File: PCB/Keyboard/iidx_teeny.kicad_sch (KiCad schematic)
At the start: 46 parts, among them J1 CONN_01x05, SW1 SWITCH_SPST, SW10 SWITCH_SPST, SW11 SWITCH_SPST, SW12 SWITCH_SPST, SW13 SWITCH_SPST, SW2 SWITCH_SPST, SW3 SWITCH_SPST, SW4 SWITCH_SPST, SW5 SWITCH_SPST, SW6 SWITCH_SPST, SW7 SWITCH_SPST, SW8 SWITCH_SPST, SW9 SWITCH_SPST, U1 Pico, U2 SN74LV1T34DBV, U3 SN74LV1T34DBV

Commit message: PCB and keyboard housing done
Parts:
- removed J1: CONN_01x05, iidx_pico:Pogo_5P_Female, symbol agg:CONN_01x05
- removed TV1, TV2, TV3: D_TVS, Diode_SMD:D_SOD-323_HandSoldering, symbol Device:D_TVS
- added J1: Conn_01x03, iidx_teeny:Solder_3P, symbol Connector_Generic:Conn_01x03
- added J2: Conn_01x04, iidx_teeny:Solder_4P, symbol Connector_Generic:Conn_01x04
- D1: renamed from D10; footprint iidx_pico:WS2812B-2835 -> iidx_teeny:WS2812B-2835; symbol iidx_pico:WS2812B_Unified -> iidx_teeny:WS2812B_Unified
- D2: renamed from D20; footprint iidx_pico:WS2812B-2835 -> iidx_teeny:WS2812B-2835; symbol iidx_pico:WS2812B_Unified -> iidx_teeny:WS2812B_Unified
- D3: renamed from D30; footprint iidx_pico:WS2812B-2835 -> iidx_teeny:WS2812B-2835; symbol iidx_pico:WS2812B_Unified -> iidx_teeny:WS2812B_Unified
- D4: renamed from D40; footprint iidx_pico:WS2812B-2835 -> iidx_teeny:WS2812B-2835; symbol iidx_pico:WS2812B_Unified -> iidx_teeny:WS2812B_Unified
- D5: renamed from D50; footprint iidx_pico:WS2812B-2835 -> iidx_teeny:WS2812B-2835; symbol iidx_pico:WS2812B_Unified -> iidx_teeny:WS2812B_Unified
- D6: renamed from D60; footprint iidx_pico:WS2812B-2835 -> iidx_teeny:WS2812B-2835; symbol iidx_pico:WS2812B_Unified -> iidx_teeny:WS2812B_Unified
- D7: renamed from D70; footprint iidx_pico:WS2812B-2835 -> iidx_teeny:WS2812B-2835; symbol iidx_pico:WS2812B_Unified -> iidx_teeny:WS2812B_Unified
- DA1, DA2, DA3, DA4: footprint iidx_pico:WS2812B-2835 -> iidx_teeny:WS2812B-2835; symbol iidx_pico:WS2812B_Unified -> iidx_teeny:WS2812B_Unified
- SCR1, SCR2, SCR3, SCR4: footprint iidx_pico:MountingHole_3.2mm_M3 -> iidx_teeny:MountingHole_3.2mm_M3; symbol iidx_pico:ScrewHole -> iidx_teeny:ScrewHole
- U2, U3: footprint iidx_pico:SOT-23-5_Jumper -> iidx_teeny:SOT-23-5_Jumper
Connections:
- net +5V: now also J1.1 (Pin_1)
- net GND: now also J1.3 (Pin_3), J2.4 (Pin_4)
- net SCL: now also J2.2 (Pin_2)
- net SDA: now also J2.3 (Pin_3)
- net TT_LED: now also J1.2 (Pin_2)
- net 3V3: now reaches U1.36 (3V3)
- net 3V3: now also J2.1 (Pin_1)
- no-connect marks 14 -> 18
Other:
- moved on the sheet: R1, R3

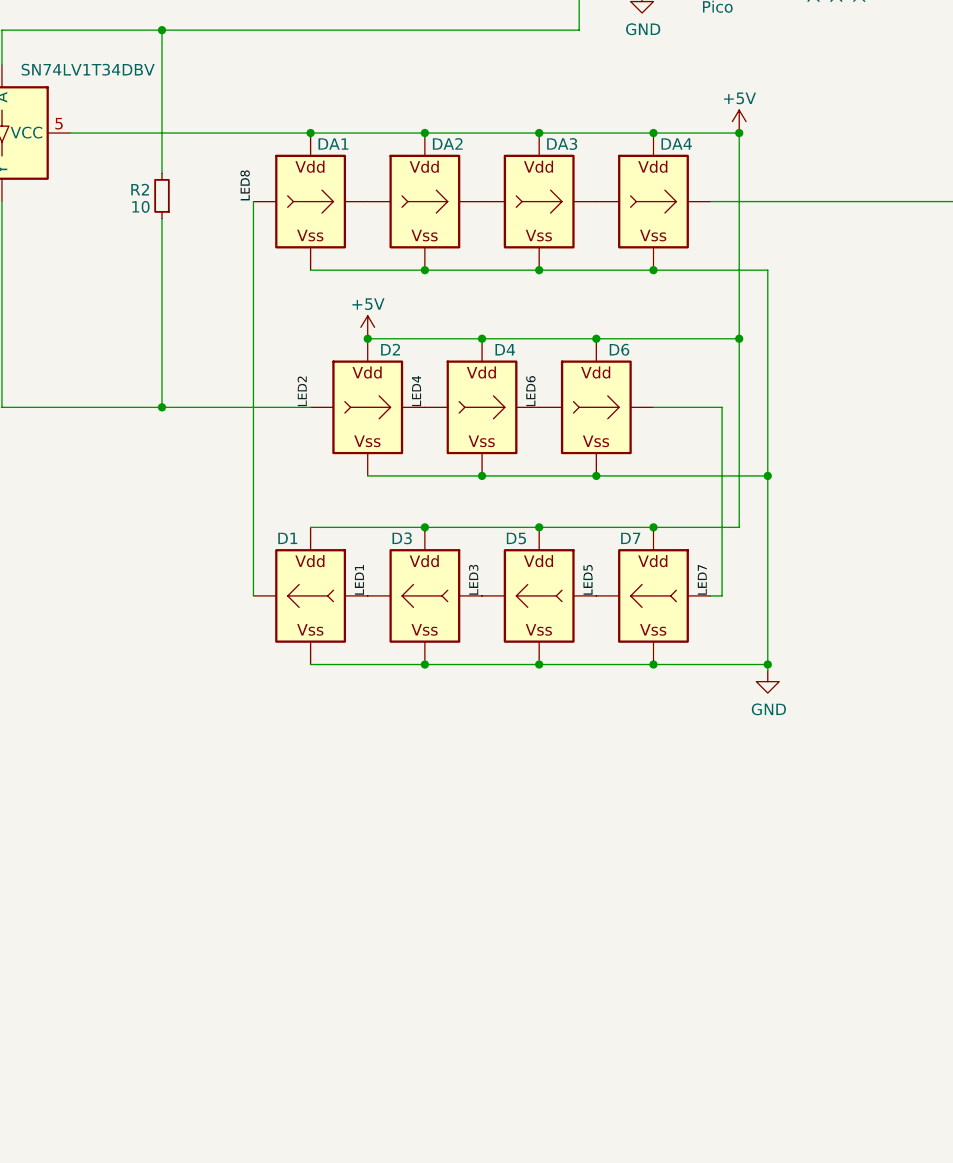
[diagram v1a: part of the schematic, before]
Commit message: PCB updated with two LEDs per button and larger Y gap
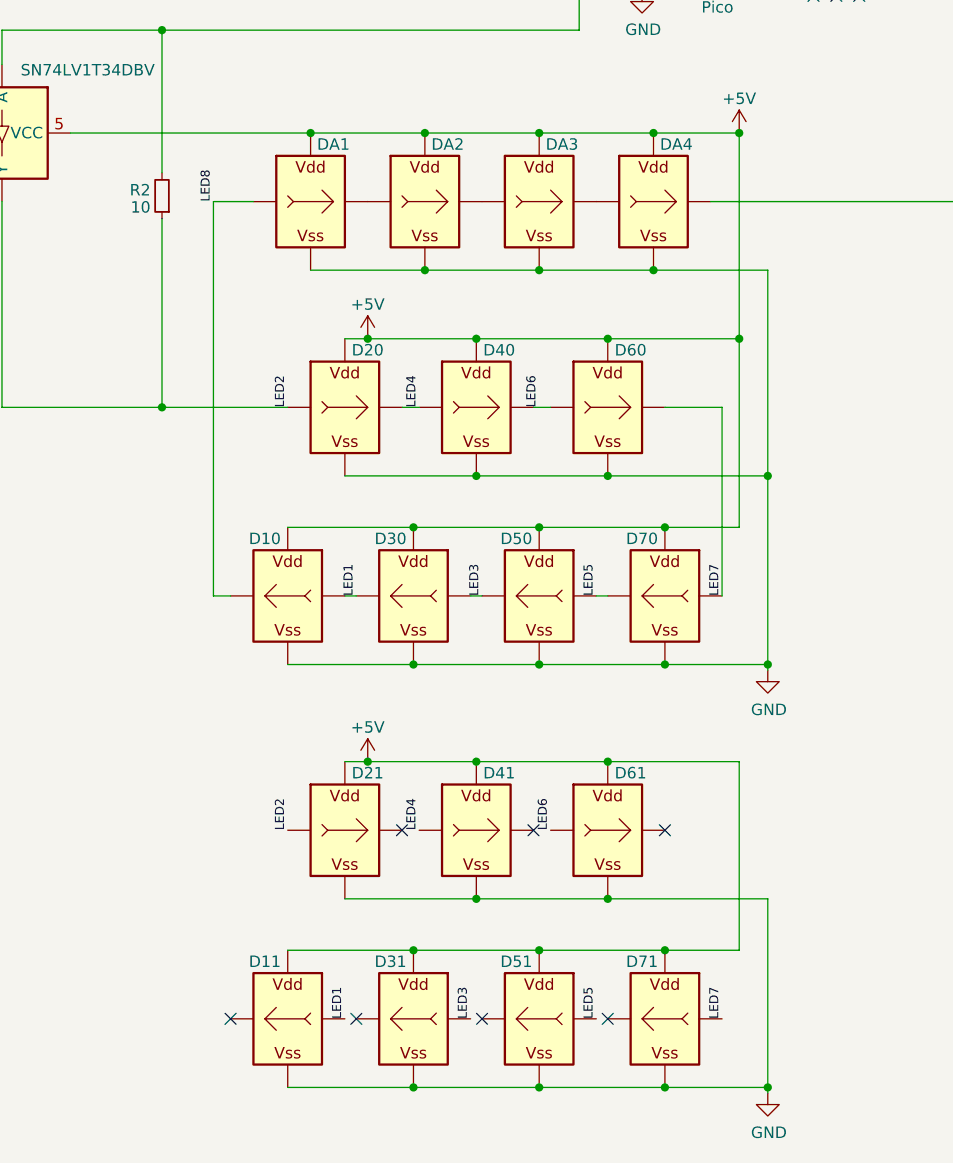
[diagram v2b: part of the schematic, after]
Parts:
- added D11, D21, D31, D41, D51, D61, D71: WS2812B_Unified, iidx_teeny:WS2812B-2835, symbol iidx_teeny:WS2812B_Unified
- renumbered D1 to D10, D2 to D20, D3 to D30, D4 to D40, D5 to D50, D6 to D60, D7 to D70
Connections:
- net +5V: now also D11.V (VDD), D21.V (VDD), D31.V (VDD), D41.V (VDD), D51.V (VDD), D61.V (VDD), D71.V (VDD)
- net GND: now also D11.G (VSS), D21.G (VSS), D31.G (VSS), D41.G (VSS), D51.G (VSS), D61.G (VSS), D71.G (VSS)
- net LED1: now also D11.I (In)
- net LED2: now also D21.I (In)
- net LED3: now also D31.I (In)
- net LED4: now also D41.I (In)
- net LED5: now also D51.I (In)
- net LED6: now also D61.I (In)
- net LED7: now also D71.I (In)
- no-connect marks 18 -> 25
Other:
- moved on the sheet: D10, D20, D30, D40, D60, D70

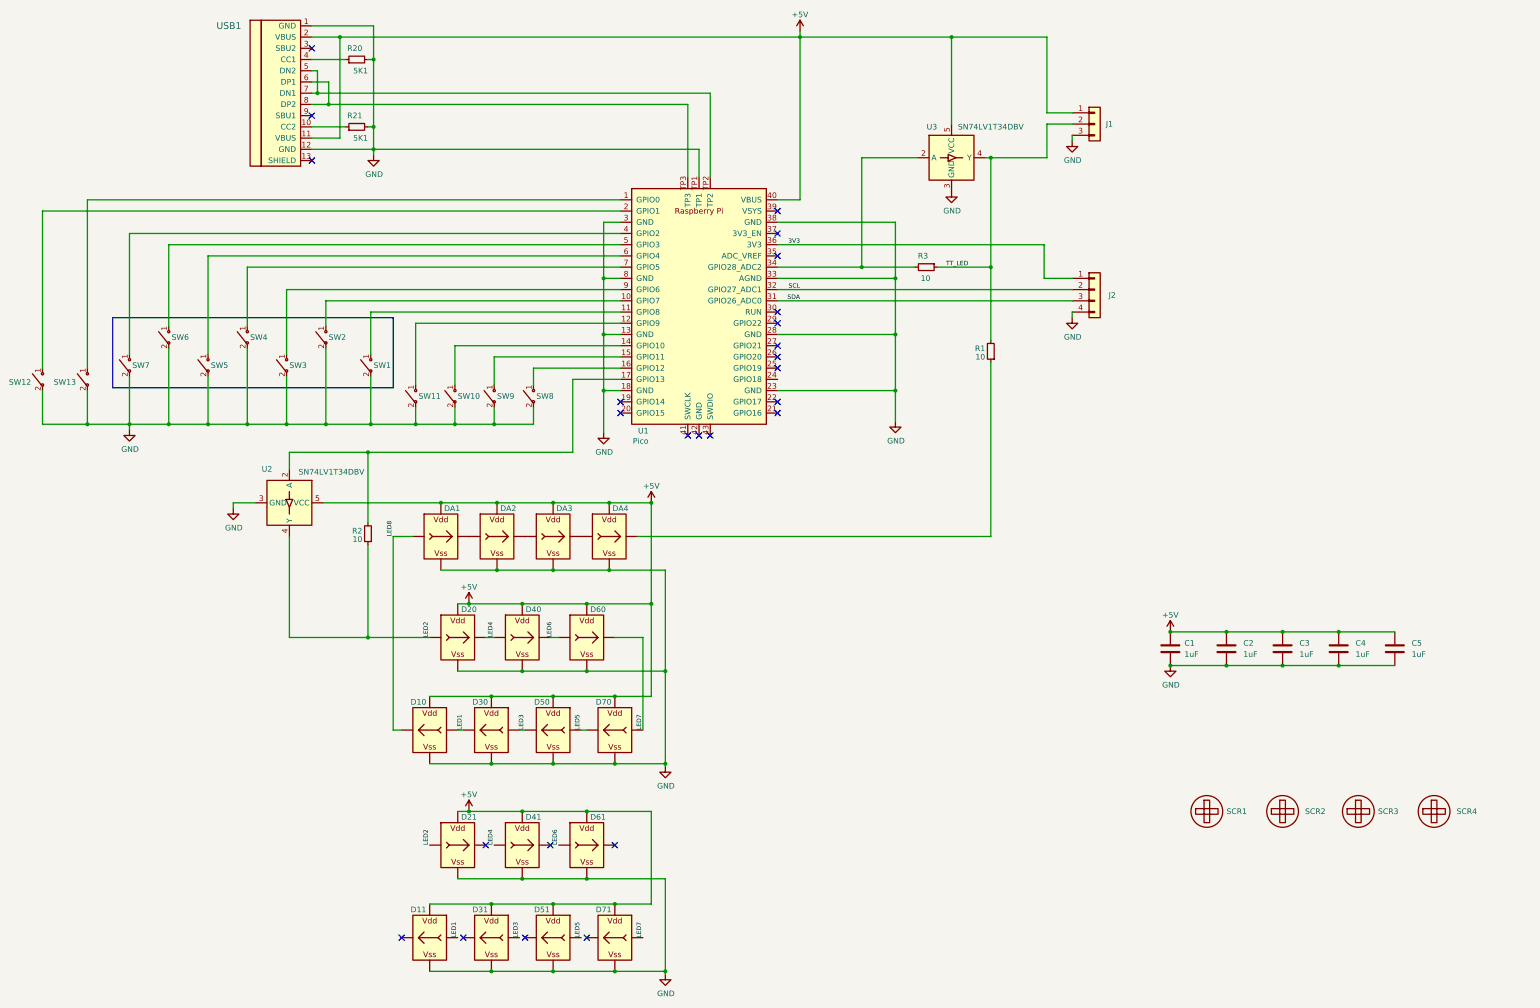
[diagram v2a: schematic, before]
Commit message: PCB v1.2, easier soldering
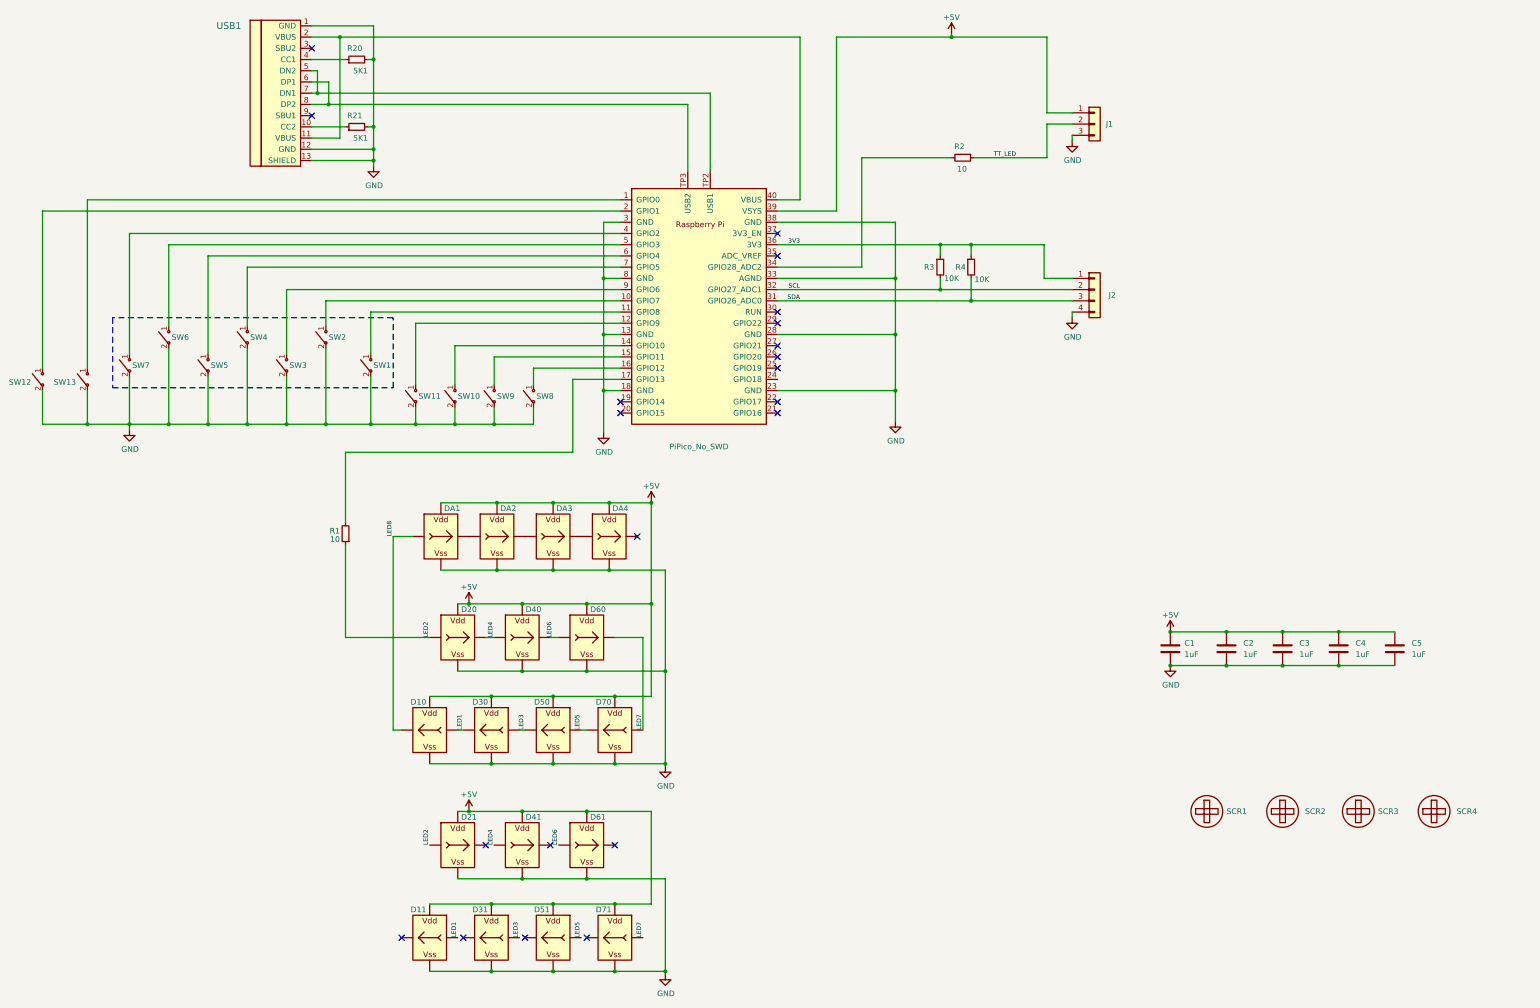
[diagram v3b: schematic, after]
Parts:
- removed R1: 10, Resistor_SMD:R_0603_1608Metric, symbol Device:R_Small
- removed U1: Pico, iidx_teeny:RPi_Pico_SMD_Pins, symbol MCU_RaspberryPi_and_Boards:Pico
- removed U2, U3: SN74LV1T34DBV, iidx_teeny:SOT-23-5_Jumper, symbol Logic_LevelTranslator:SN74LV1T34DBV
- added R3, R4: 10K, Resistor_SMD:R_0603_1608Metric_Pad0.98x0.95mm_HandSolder, symbol Device:R_Small
- added U1: PiPico_No_SWD, iidx_teeny:RPi_Pico_SMD_Pins_No_SWD_No_Text, symbol iidx_pico:PiPico_No_SWD
- R1: renamed from R2; footprint Resistor_SMD:R_0603_1608Metric -> Resistor_SMD:R_0603_1608Metric_Pad0.98x0.95mm_HandSolder
- R2: renamed from R3; footprint Resistor_SMD:R_0603_1608Metric -> Resistor_SMD:R_0603_1608Metric_Pad0.98x0.95mm_HandSolder
- R20, R21: footprint Resistor_SMD:R_0603_1608Metric -> Resistor_SMD:R_0603_1608Metric_Pad0.98x0.95mm_HandSolder
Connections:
- net +5V: now also U1.39 (VSYS); no longer USB1.11 (VBUS), USB1.2 (VBUS)
- net 3V3: now also R3.1, R4.1, U1.36 (3V3)
- net GND: now also USB1.13 (SHIELD), U1.13 (GND), U1.18 (GND), U1.23 (GND), U1.28 (GND), U1.3 (GND), U1.33 (AGND), U1.38 (GND), U1.8 (GND)
- net SCL: now also R3.2, U1.32 (GPIO27_ADC1)
- net SDA: now also R4.2, U1.31 (GPIO26_ADC0)
- net at SW13.1 ("~{"}): now also U1.1 (GPIO0)
- net at SW2.1 ("~{"}): now also U1.10 (GPIO7)
- net at SW1.1 ("~{"}): now also U1.11 (GPIO8)
- net at SW11.1 ("~{"}): now also U1.12 (GPIO9)
- net at SW10.1 ("~{"}): now also U1.14 (GPIO10)
- net at SW9.1 ("~{"}): now also U1.15 (GPIO11)
- net at SW8.1 ("~{"}): now also U1.16 (GPIO12)
- net at R1.2: now also U1.17 (GPIO13)
- net at SW12.1 ("~{"}): now also U1.2 (GPIO1)
- net at R2.2: now also U1.34 (GPIO28_ADC2)
- net at SW7.1 ("~{"}): now also U1.4 (GPIO2)
- net at SW6.1 ("~{"}): now also U1.5 (GPIO3)
- net at SW5.1 ("~{"}): now also U1.6 (GPIO4)
- net at SW4.1 ("~{"}): now also U1.7 (GPIO5)
- net at SW3.1 ("~{"}): now also U1.9 (GPIO6)
- net at USB1.5 (DN2), USB1.7 (DN1): now also U1.TP2 (USB1)
- net at USB1.6 (DP1), USB1.8 (DP2): now also U1.TP3 (USB2)
- new net: U1.40 (VBUS), USB1.11 (VBUS), USB1.2 (VBUS)
- no-connect marks 25 -> 21
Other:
- moved on the sheet: R1, R2

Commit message: PCB v1.3 (sensors on board)
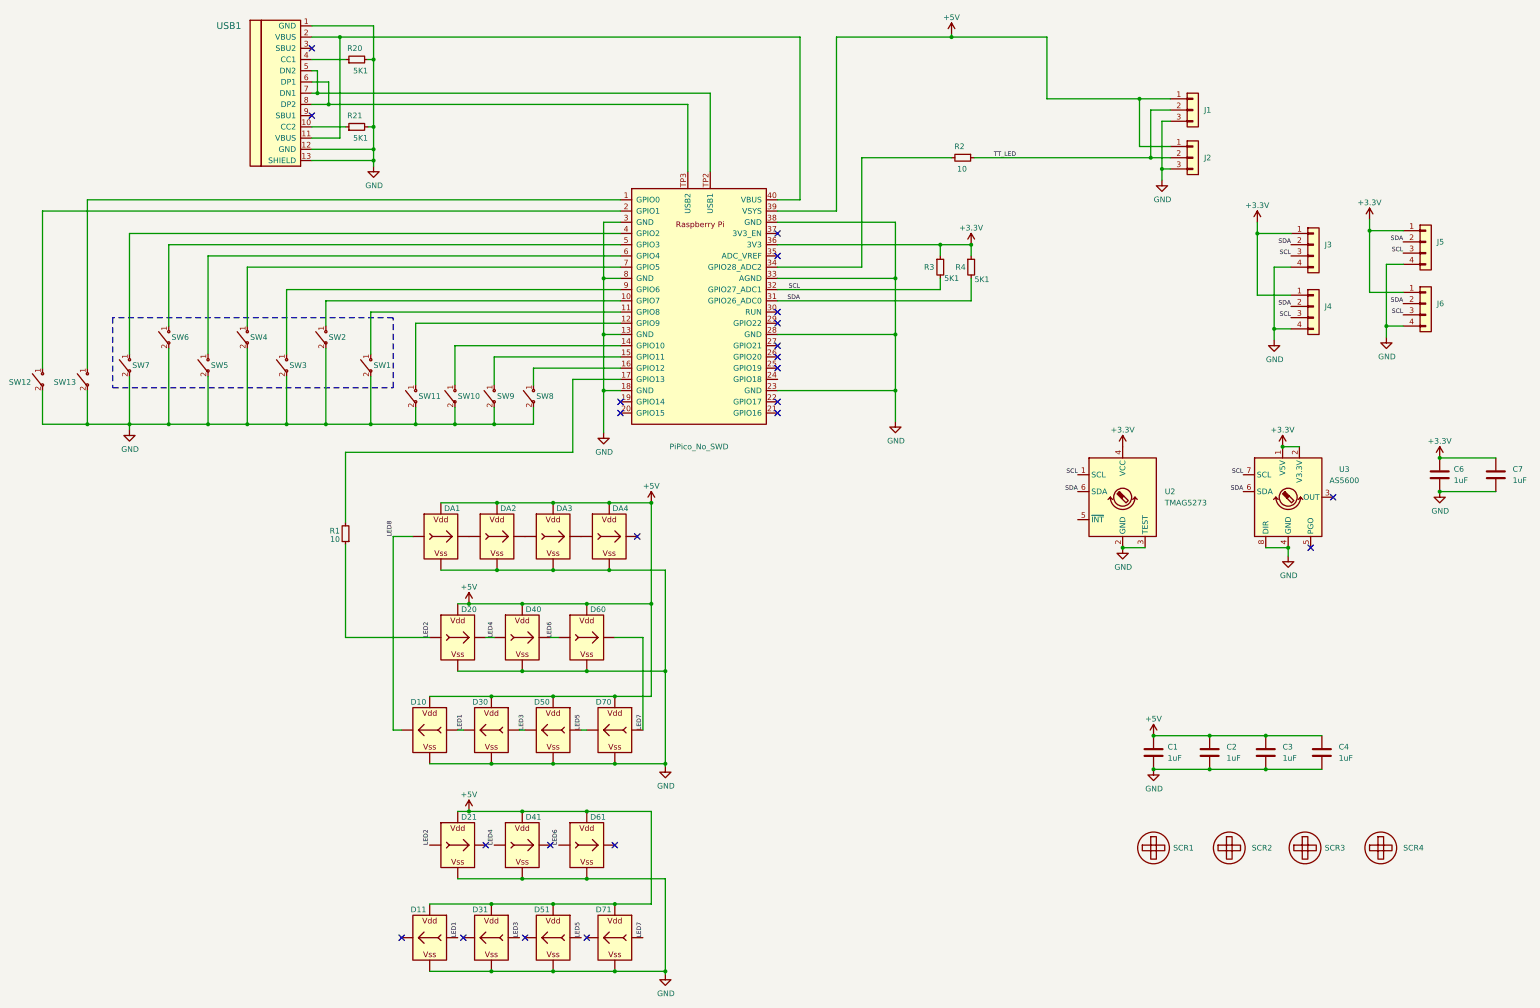
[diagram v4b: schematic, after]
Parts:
- removed C5: 1uF, Capacitor_SMD:C_0805_2012Metric, symbol Device:C
- removed J2: Conn_01x04, iidx_teeny:Solder_4P, symbol Connector_Generic:Conn_01x04
- added C6, C7: 1uF, Capacitor_SMD:C_0603_1608Metric_Pad1.08x0.95mm_HandSolder, symbol Device:C
- added J2: RGB, iidx_teeny:SH1.0_3P_Solder_Combo, symbol Connector_Generic:Conn_01x03
- added J3, J4: Spin, iidx_teeny:SH1.0_4P_Solder_Combo, symbol Connector_Generic:Conn_01x04
- added J5, J6: Spin, iidx_teeny:P2.0_4P_Solder, symbol Connector_Generic:Conn_01x04
- added U2: TMAG5273, Package_TO_SOT_SMD:TSOT-23-6_HandSoldering, symbol iidx_teeny:TMAG5273
- added U3: AS5600, Package_SO:SOIC-8_3.9x4.9mm_P1.27mm, symbol iidx_teeny:AS5600
- C1, C2, C3, C4: footprint Capacitor_SMD:C_0805_2012Metric -> Capacitor_SMD:C_0603_1608Metric_Pad1.08x0.95mm_HandSolder
- J1: value Conn_01x03 -> RGB; footprint iidx_teeny:Solder_3P -> iidx_teeny:SH1.0_3P_Solder_Combo
- R3, R4: value 10K -> 5K1
- U1: symbol iidx_pico:PiPico_No_SWD -> iidx_teeny:PiPico_No_SWD
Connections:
- net +5V: now also J2.1 (Pin_1)
- net GND: now also C6.2, C7.2, J2.3 (Pin_3), J3.4 (Pin_4), J4.4 (Pin_4), J5.4 (Pin_4), J6.4 (Pin_4), U2.2 (GND), U2.3 (TEST), U3.4 (GND), U3.8 (DIR)
- net SCL: now also J3.3 (Pin_3), J4.3 (Pin_3), J5.3 (Pin_3), J6.3 (Pin_3), U2.1 (SCL), U3.7 (SCL)
- net SDA: now also J3.2 (Pin_2), J4.2 (Pin_2), J5.2 (Pin_2), J6.2 (Pin_2), U2.6 (SDA), U3.6 (SDA)
- net TT_LED: now also J2.2 (Pin_2)
- net 3V3 renamed +3.3V
- net +3.3V: now also C6.1, C7.1, J3.1 (Pin_1), J4.1 (Pin_1), J5.1 (Pin_1), J6.1 (Pin_1), U2.4 (VCC), U3.1 (V5V), U3.2 (V3.3V)
- no-connect marks 21 -> 23
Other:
- moved on the sheet: C1, C2, C3, C4, SCR1, SCR2, SCR3, SCR4
